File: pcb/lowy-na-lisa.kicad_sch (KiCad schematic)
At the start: 52 parts, among them J1 Display, J3 USB_C_Receptacle_USB2.0_16P, Q1 AO3400A, Q2 AO3400A, SW1 TS24CA, SW2 TS24CA, SW3 TS24CA, SW4 TS24CA, U1 TPS61022, U2 TP4054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

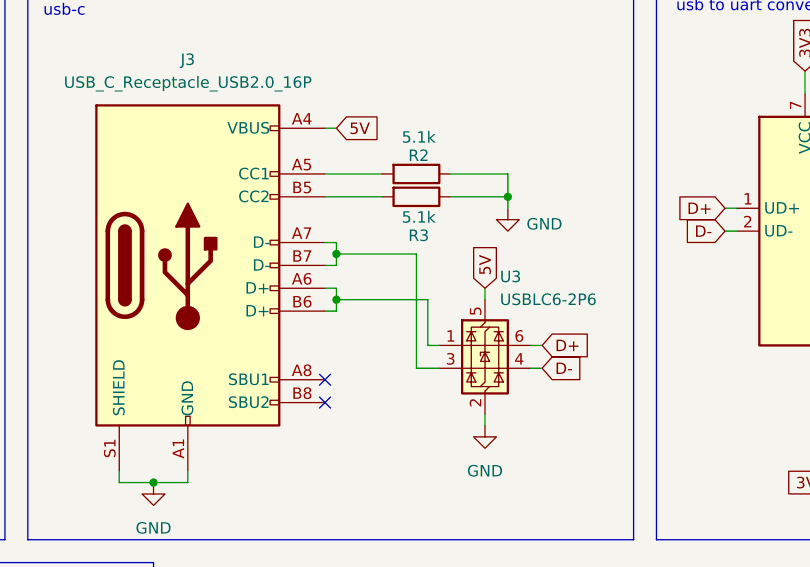
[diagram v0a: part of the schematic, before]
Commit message: pcb: rename project, final touches, cleanup
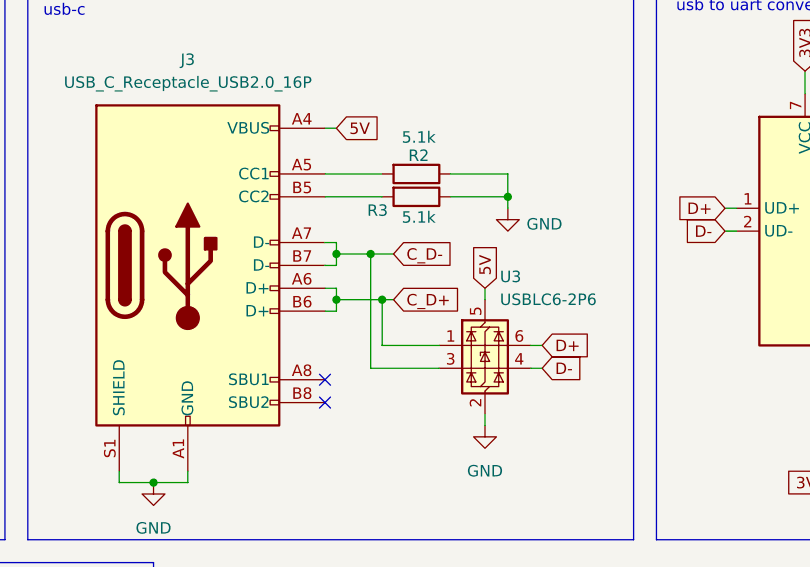
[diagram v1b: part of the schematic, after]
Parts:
- HTCC-AM1: symbol New_Library:HTCC-AM01 -> library:HTCC-AM01
- SW1, SW2, SW3, SW4: symbol Switch:SW_Omron_B3FS -> Switch:SW_Push
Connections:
- net C_D+: now reaches J3.A6 (D+), J3.B6 (D+), U3.1 (I/O1)
- net C_D-: now reaches J3.A7 (D-), J3.B7 (D-), U3.3 (I/O2)
